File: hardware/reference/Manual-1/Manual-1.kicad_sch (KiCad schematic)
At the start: 25 parts, among them J1 DCC, J2 ICSP, J3 TTL Serial, U1 6N137, U21 PIC18F06Q40-I/P

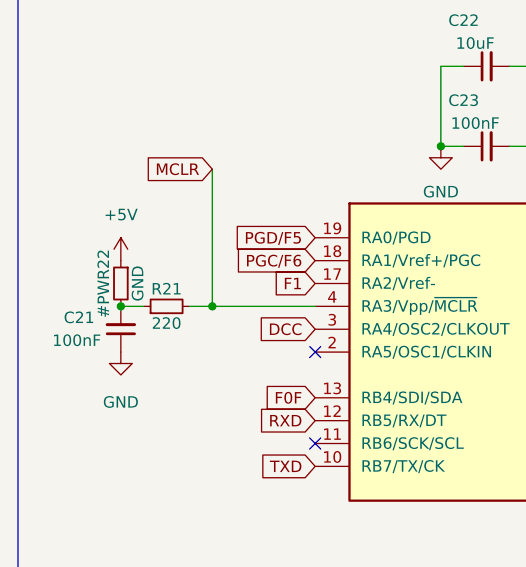
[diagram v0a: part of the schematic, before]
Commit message: Minor tweak to BOM.
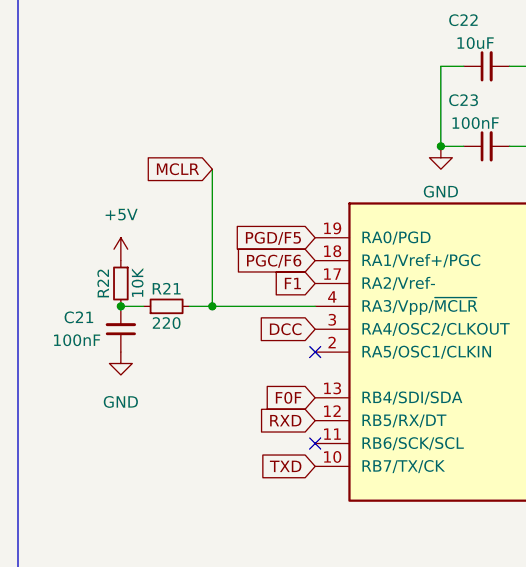
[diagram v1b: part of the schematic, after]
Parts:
- R22: renamed from #PWR22; value GND -> 10K
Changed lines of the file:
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@@
   (symbol (lib_id "Device:R_Small") (at 26.67 57.15 0) (mirror y) (unit 1)
     (in_bom yes) (on_board yes)
-    (property "Reference" "#PWR22" (id 0) (at 24.765 57.15 90))
-    (property "Value" "GND" (id 1) (at 28.575 57.15 90))
+    (property "Reference" "R22" (id 0) (at 24.765 57.15 90))
+    (property "Value" "10K" (id 1) (at 28.575 57.15 90))
     (property "Footprint" "Resistor_SMD:R_0402_1005Metric" (id 2) (at 26.67 57.15 0)
       (effects (font (size 1.27 1.27)) hide)
@@
       (reference "#PWR021") (unit 1) (value "+5V") (footprint "")
     )
-    (path "/9ee7b1d5-1d4a-457a-868f-1c5ac3f6e002"
-      (reference "#PWR22") (unit 1) (value "GND") (footprint "Resistor_SMD:R_0402_1005Metric")
-    )
     (path "/a5f90bef-a137-498d-948d-351928295469"
       (reference "#PWR023") (unit 1) (value "GND") (footprint "")
@@
       (reference "R21") (unit 1) (value "220") (footprint "Resistor_THT:R_Radial_Power_L7.0mm_W8.0mm_Px2.40mm_Py2.30mm")
     )
+    (path "/9ee7b1d5-1d4a-457a-868f-1c5ac3f6e002"
+      (reference "R22") (unit 1) (value "10K") (footprint "Resistor_SMD:R_0402_1005Metric")
+    )
     (path "/b9faa690-021f-46a9-825e-888b17a3e0e8"
